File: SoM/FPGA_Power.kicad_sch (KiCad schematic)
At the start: 42 parts, among them U1 CCGM1A1

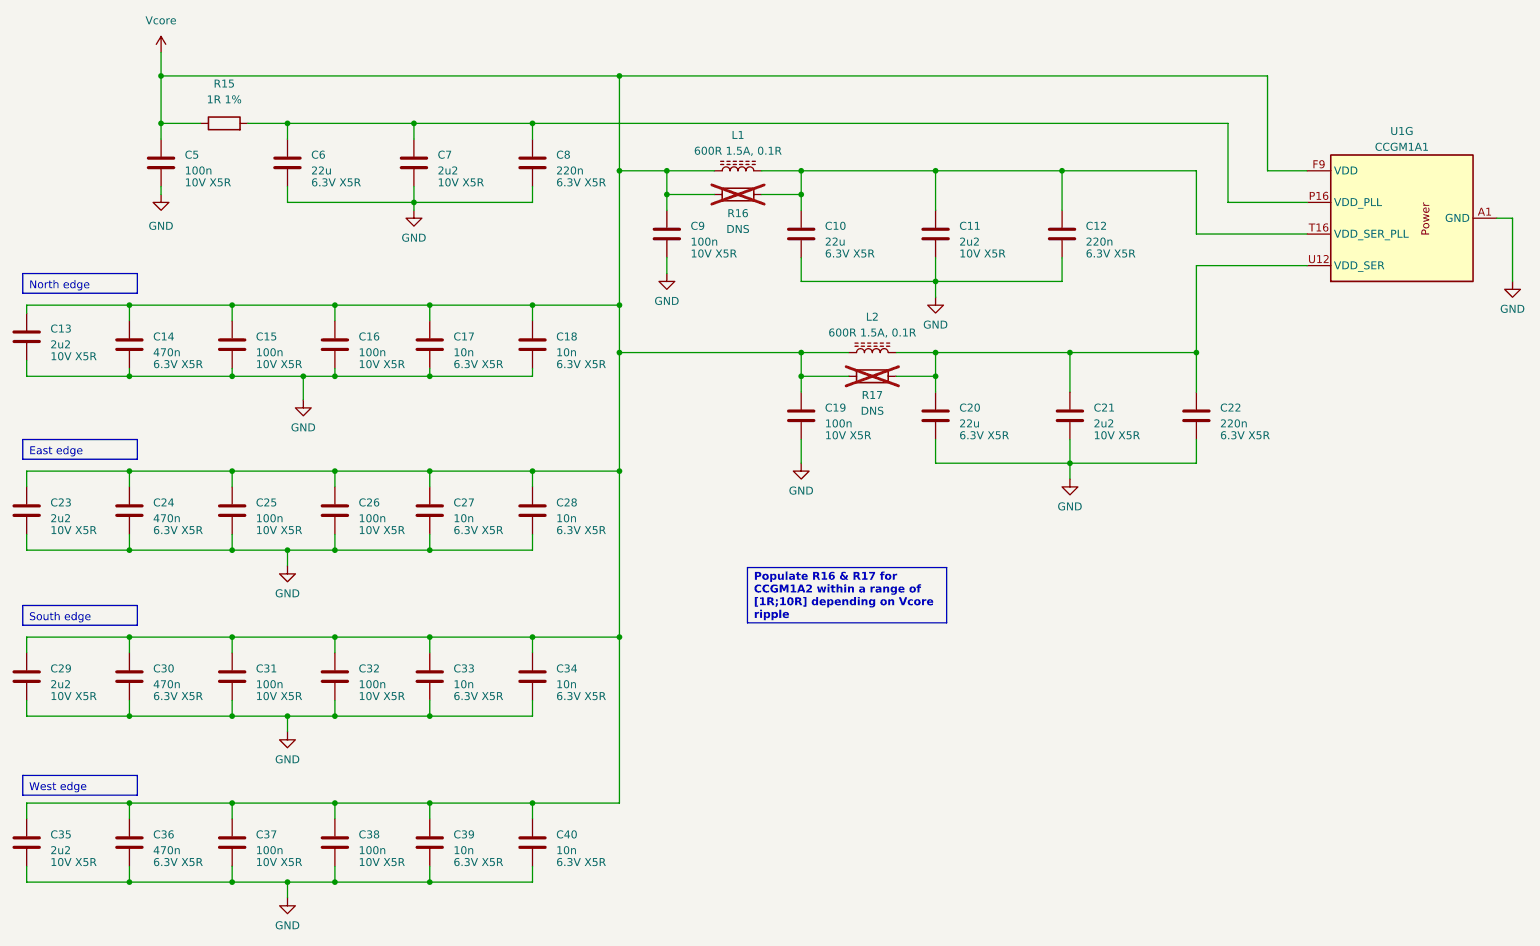
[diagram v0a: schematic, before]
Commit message: Created Version with 0402 components
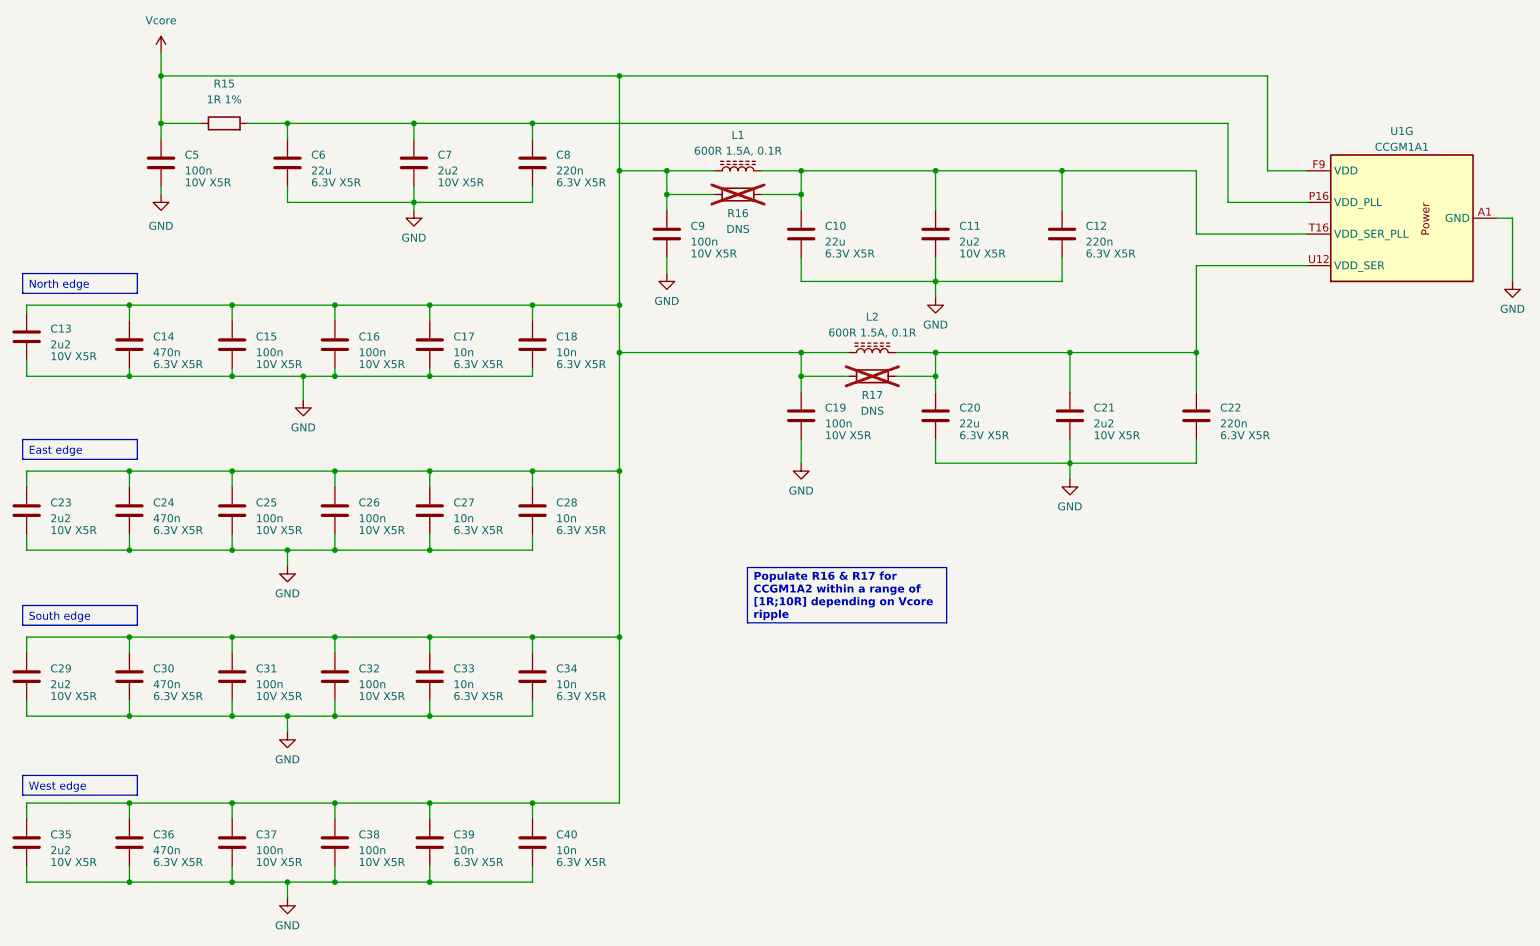
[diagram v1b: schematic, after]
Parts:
- C10, C20, C6: Mouser Part Number 187-CL10A226KQ8NRNE -> GRM188C61C226ME01W; Part Number (none) -> GRM188C61C226ME01W
- C11, C13, C21, C23, C29, C35, C7: footprint Capacitor_SMD:C_0201_0603Metric -> Capacitor_SMD:C_0402_1005Metric; Mouser Part Number 187-CL03A225KP3CRNC -> GRM155Z71A225KE44D; Part Number (none) -> GRM155Z71A225KE44D
- C12, C22, C8: footprint Capacitor_SMD:C_0201_0603Metric -> Capacitor_SMD:C_0402_1005Metric; Mouser Part Number 187-CL03A224KQ3NNNC -> GRM155R71C224KA12D; Part Number (none) -> GRM155R71C224KA12D
- C14, C24, C30, C36: footprint Capacitor_SMD:C_0201_0603Metric -> Capacitor_SMD:C_0402_1005Metric; Mouser Part Number 187-CL03A474KQ3NNNH -> GRT155C81C474KE01D; Part Number (none) -> GRT155C81C474KE01D
- C15, C16, C19, C25, C26, C31, C32, C37, C38, C5, C9: footprint Capacitor_SMD:C_0201_0603Metric -> Capacitor_SMD:C_0402_1005Metric; Mouser Part Number 187-CL03A104KP3NNNC -> GRM155R71C104KA88J; Part Number (none) -> GRM155R71C104KA88J
- C17, C18, C27, C28, C33, C34, C39, C40: footprint Capacitor_SMD:C_0201_0603Metric -> Capacitor_SMD:C_0402_1005Metric; Mouser Part Number 187-CL03B103KOSVPNC -> GRM155R71C103KA01D; Part Number (none) -> GRM155R71C103KA01D
- L1, L2: Mouser Part Number 710-74269262601 -> 74269262601; Part Number (none) -> 74269262601
- R15: footprint Resistor_SMD:R_0201_0603Metric -> Resistor_SMD:R_0402_1005Metric; Mouser Part Number 71-CRCW02011R00FXED -> CRCW04021R00FKEDHP; Part Number (none) -> CRCW04021R00FKEDHP
- R16, R17: footprint Resistor_SMD:R_0201_0603Metric -> Resistor_SMD:R_0402_1005Metric
- U1: Mouser Part Number (none) -> CCGM1A1-BGA324; Part Number (none) -> CCGM1A1-BGA324
